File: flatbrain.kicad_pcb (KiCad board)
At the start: 2 copper layers, 272.2 x 143 mm, 108 parts, among them J1 OLED, SW1 SW_Push, SW41 Rotary_Encoder_Switch, SW42 Rotary_Encoder_Switch, U1 Elite-C

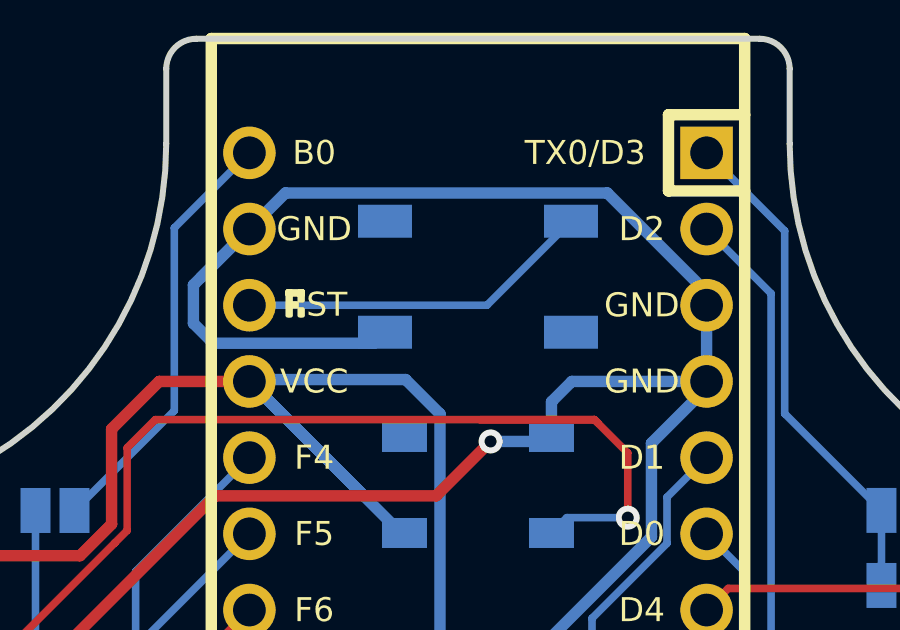
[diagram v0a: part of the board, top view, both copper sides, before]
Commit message: Remove gerber file
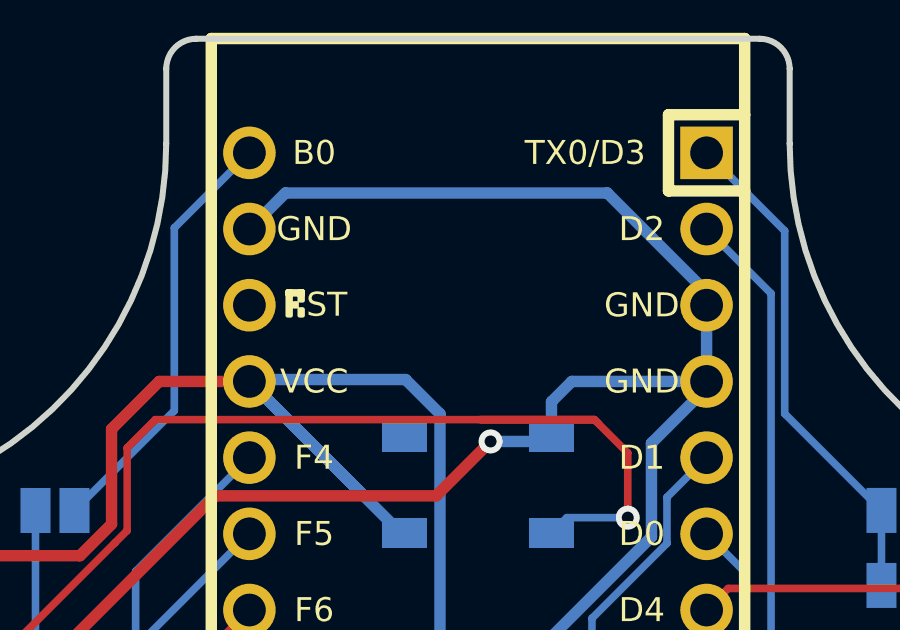
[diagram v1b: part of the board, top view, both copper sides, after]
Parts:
- removed SW1: SW_Push, random-keyboard-parts:SKQG-1155865
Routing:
- net GND: track 835.1 -> 821.6 mm
- net RST: track 11.9 -> 0.00 mm

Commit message: Update the outline with the new design
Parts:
- moved D46 17.2 mm to (221.4, 96.0)
- moved D40 17.2 mm to (120.0, 137.6)
- moved D37 16.7 mm to (74.4, 96.0)
- moved D35 13.1 mm to (247.3, 69.6), turned to 208 degrees
- moved D36 11.3 mm to (264.1, 60.7), turned to 208 degrees
- moved D25 11.2 mm to (31.7, 60.7), turned to 332 degrees
- moved LED7 7.64 mm to (32.1, 75.9)
- moved LED3 7.17 mm to (263.7, 75.9)
- moved LED6 3.94 mm to (85.2, 108.3)
- moved LED4 3.72 mm to (210.6, 108.3)
- moved LED5 1.92 mm to (147.9, 141.9)
- moved D3 0.95 mm to (92.7, 40.4)
- moved MX39 0.95 mm to (112.9, 127.6)
- moved J1 0.95 mm to (151.7, 53.1)
- moved D5 0.95 mm to (126.1, 58.7)
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- renumbered JP1 to Elite-c, JP2 to Elite-c, JP3 to Pro-micro
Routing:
- net GND: track 821.6 -> 799.8 mm
- net ROW3: track 299.4 -> 317.9 mm
- net Net-(D36-Pad2): track 11.3 -> 3.44 mm
- net VCC: track 701.1 -> 693.7 mm
- net Net-(LED2-Pad2): track 65.9 -> 59.2 mm
- net Net-(LED5-Pad2): track 90.7 -> 85.2 mm
- net Net-(D46-Pad2): track 11.3 -> 6.20 mm
- net Net-(D37-Pad2): track 6.20 -> 11.3 mm
- net Net-(D40-Pad2): track 6.20 -> 11.3 mm
- net COL0: track 147.7 -> 143.6 mm
- net Net-(LED8-Pad2): track 60.7 -> 56.9 mm
- net ROW2: track 371.5 -> 375.2 mm
- net Net-(D25-Pad2): track 7.25 -> 3.97 mm
- net Net-(D35-Pad2): track 6.20 -> 3.44 mm
- net COL3: track 149.5 -> 152.0 mm
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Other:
- board size 272.2 x 143 mm -> 268.7 x 141.1 mm

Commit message: Add choc support
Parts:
- MX1, MX10, MX11, MX12, MX13, MX14, MX15, MX16, MX17, MX18, MX19, MX2, MX20, MX21, MX22, MX23, MX24, MX25, MX26, MX27, MX28, MX29, MX3, MX30, MX31, MX32, MX33, MX34, MX35, MX36, MX37, MX38, MX39, MX4, MX40, MX43, MX44, MX45, MX46, MX5, MX6, MX7, MX8, MX9: footprint parts:mx_1u -> parts:mxchoc_1u
- SW41, SW42: footprint parts:rotary_x_mx -> parts:rotary_x_mxchoc
- moved MX22 3.61 mm to (219.0, 56.9)
- moved LED3 3.61 mm to (263.4, 79.5)
- moved MX13 3.61 mm to (34.7, 53.8)
- moved D10 3.61 mm to (217.3, 36.2)
- moved MX37 3.61 mm to (81.4, 103.4)
- moved D29 3.61 mm to (107.9, 96.0)
- moved D44 3.61 mm to (187.5, 124.6)
- moved D6 3.61 mm to (141.5, 73.4)
- moved D28 3.61 mm to (94.1, 81.3)
- moved MX27 3.61 mm to (67.2, 73.8)
- moved MX33 3.61 mm to (208.3, 77.4)
- moved D26 3.61 mm to (49.9, 83.4)
- moved D5 3.61 mm to (125.8, 62.3)
- moved D8 3.61 mm to (183.9, 54.6)
- moved MX20 3.61 mm to (185.6, 75.3)
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- renumbered Elite-c to elite-c, Pro-micro to pro-micro
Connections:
- net RST renamed Net-(U1-Pad22)
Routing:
- net COL4: track 132.3 -> 162.5 mm
- net Net-(LED8-Pad2): track 56.9 -> 83.3 mm
- net COL1: track 174.9 -> 198.2 mm
- net COL8: track 144.8 -> 165.9 mm
- net COL5: track 87.1 -> 105.6 mm
- net COL6: track 86.9 -> 105.2 mm
- net COL7: track 127.1 -> 145.1 mm
- net COL9: track 151.9 -> 169.2 mm
- net COL10: track 174.9 -> 191.2 mm
- net COL11: track 138.7 -> 154.9 mm
- net COL2: track 159.9 -> 175.4 mm
- net COL3: track 152.0 -> 166.7 mm
- net COL0: track 143.6 -> 154.7 mm
- net ROW1: track 331.4 -> 341.8 mm
- net Net-(LED2-Pad2): track 59.2 -> 67.1 mm
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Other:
- outline, holes or cut-outs redrawn

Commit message: wip: switches placed, matrix change
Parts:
- removed D31, D40, D41, D42, D43, D44, D45, D46: D_Small, Keebio-Parts:Diode-Hybrid-Back
- removed the D38 at (104.8, 121.5)
- removed MX31, MX35, MX36, MX40, MX43, MX44, MX45, MX46: MX-NoLED, parts:mxchoc_1u
- removed SW41, SW42: Rotary_Encoder_Switch, parts:rotary_x_mxchoc
- removed elite-c (x2), pro-micro: Jumper_NO_Small, Jumper:SolderJumper-2_P1.3mm_Open_Pad1.0x1.5mm
- added D38: D_Small, Keebio-Parts:Diode-dual, F.Cu at (315.5, 104.4)
- added D38: D_Small, Keebio-Parts:Diode-dual, F.Cu at (294.7, 99.1)
- D1, D10, D11, D12, D13, D14, D15, D16, D17, D18, D19, D2, D20, D21, D22, D23, D24, D25, D26, D27, D28, D29, D3, D30, D32, D33, D34, D35, D36, D37, D39, D4, D5, D6, D7, D8, D9: footprint Keebio-Parts:Diode-Hybrid-Back -> Keebio-Parts:Diode-dual
- MX1, MX10, MX11, MX12, MX13, MX14, MX15, MX16, MX17, MX18, MX19, MX2, MX20, MX21, MX22, MX23, MX24, MX25, MX26, MX27, MX28, MX29, MX3, MX30, MX32, MX33, MX34, MX37, MX38, MX39, MX4, MX5, MX6, MX7, MX8, MX9: footprint parts:mxchoc_1u -> parts:mix_1u
- U1: moved to F.Cu
- moved D13 328.8 mm to (367.5, 104.4), turned to 0 degrees
- moved D14 321.0 mm to (377.9, 101.7), turned to 0 degrees
- moved D26 307.6 mm to (357.1, 99.1), turned to 0 degrees
- moved D25 307.5 mm to (336.3, 104.4), turned to 0 degrees
- moved D15 296.9 mm to (377.9, 99.1), turned to 0 degrees
- moved LED8 281.3 mm to (329.4, 77.0), turned to 0 degrees
- moved D1 279.8 mm to (325.9, 99.1), turned to 0 degrees
- moved D27 273.2 mm to (346.7, 101.7), turned to 0 degrees
- moved LED7 270.6 mm to (302.4, 82.5), turned to 0 degrees
- moved D28 263.7 mm to (357.1, 101.7), turned to 0 degrees
- moved D2 241.1 mm to (305.1, 99.1), turned to 0 degrees
- moved LED9 234.0 mm to (330.2, 65.1), turned to 0 degrees
- moved D3 229.8 mm to (315.5, 99.1), turned to 0 degrees
- moved D16 223.3 mm to (321.8, 19.3), turned to 0 degrees
- moved D30 223.2 mm to (346.7, 99.1), turned to 0 degrees
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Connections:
- D11 pad 1: ROW0 -> ROW1
- D12 pad 1: ROW0 -> ROW1
- D21 pad 1: ROW1 -> ROW2
- D22 pad 1: ROW1 -> ROW2
- D23 pad 1: ROW1 -> ROW2
- D24 pad 1: ROW1 -> ROW2
- D32 pad 1: ROW2 -> ROW3
- D33 pad 1: ROW2 -> ROW3
- D34 pad 1: ROW2 -> ROW3
- D35 pad 1: ROW2 -> ROW3
- D36 pad 1: ROW2 -> ROW3
- MX11 pad 1: COL10 -> COL0
- MX12 pad 1: COL11 -> COL1
- MX13 pad 1: COL0 -> COL2
- MX14 pad 1: COL1 -> COL3
- MX15 pad 1: COL2 -> COL4
- MX16 pad 1: COL3 -> COL5
- MX17 pad 1: COL4 -> COL6
- MX18 pad 1: COL5 -> COL7
- MX19 pad 1: COL6 -> COL8
- MX20 pad 1: COL7 -> COL9
- MX21 pad 1: COL8 -> COL0
- MX22 pad 1: COL9 -> COL1
- MX23 pad 1: COL10 -> COL2
- MX24 pad 1: COL11 -> COL3
- MX25 pad 1: COL0 -> COL4
- MX26 pad 1: COL1 -> COL5
- MX27 pad 1: COL2 -> COL6
- MX28 pad 1: COL3 -> COL7
- MX29 pad 1: COL4 -> COL8
- MX30 pad 1: COL5 -> COL9
- MX32 pad 1: COL7 -> COL1
- MX33 pad 1: COL8 -> COL2
- MX34 pad 1: COL9 -> COL3
- MX37 pad 1: COL1 -> COL6
- MX38 pad 1: COL2 -> COL7
- MX39 pad 1: COL3 -> COL8
- U1 pad 1: Net-(JP2-Pad2) -> LED
- U1 pad 7: COL11 -> ROW0
- U1 pad 8: COL10 -> Net-(U1-Pad8)
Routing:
- net GND: track 797.5 -> 0.00 mm, vias 2 -> 0
- net VCC: track 693.6 -> 0.00 mm, vias 1 -> 0
- net ROW2: track 378.1 -> 0.00 mm, vias 1 -> 0
- net ROW1: track 341.8 -> 0.00 mm, vias 1 -> 0
- net ROW3: track 320.2 -> 0.00 mm, vias 1 -> 0
- net ROW0: track 303.9 -> 0.00 mm
- net COL1: track 198.2 -> 0.00 mm
- net COL10: track 191.2 -> 0.00 mm
- net COL2: track 175.4 -> 0.00 mm
- net COL9: track 169.2 -> 0.00 mm
- net COL3: track 166.7 -> 0.00 mm
- net COL8: track 165.9 -> 0.00 mm
- net COL4: track 162.5 -> 0.00 mm
- net COL11: track 154.9 -> 0.00 mm
- net COL0: track 154.7 -> 0.00 mm
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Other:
- board size 268.7 x 141.1 mm -> 239 x 128.4 mm
- board text removed: "Designed by louckousse"
- board text removed: "JLCJLCJLCJLC"

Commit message: everything is placed
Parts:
- removed D36: D_Small, Keebio-Parts:Diode-dual
- removed the D38 at (315.5, 104.4)
- removed the D38 at (294.7, 99.1)
- added D38: D_Small, Keebio-Parts:Diode-dual, F.Cu at (229.4, 114.2)
- added J2: Conn_01x05, Kicad-Footprints:pimoroni_trackball, F.Cu at (161.8, 114.7)
- added SW1: Rotary_Encoder_Switch, parts:rotary_x_mx, F.Cu at (134.6, 124.6)
- U1: moved to B.Cu
- moved D24 316.4 mm to (61.5, 108.5), turned to 242 degrees
- moved D22 311.3 mm to (56.2, 105.7), turned to 242 degrees
- moved D23 308.7 mm to (58.9, 107.1), turned to 242 degrees
- moved D14 298.0 mm to (79.9, 105.9), turned to 242 degrees
- moved D15 295.4 mm to (82.6, 107.3), turned to 242 degrees
- moved D21 290.6 mm to (53.6, 104.3), turned to 242 degrees
- moved D13 290.2 mm to (77.3, 104.4), turned to 242 degrees
- moved LED8 283.5 mm to (48.8, 117.1), turned to 332 degrees
- moved D12 282.4 mm to (74.6, 103.0), turned to 242 degrees
- moved LED9 282.1 mm to (48.8, 46.0), turned to 62 degrees
- moved D25 272.2 mm to (64.2, 109.9), turned to 242 degrees
- moved D32 269.6 mm to (66.8, 111.3), turned to 242 degrees
- moved D1 267.2 mm to (58.8, 94.6), turned to 242 degrees
- moved D34 264.6 mm to (72.1, 114.2), turned to 242 degrees
- moved D33 256.6 mm to (69.5, 112.7), turned to 242 degrees
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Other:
- board size 239 x 128.4 mm -> 249.8 x 129.3 mm

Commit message: first half done
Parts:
- D1, D11, D12, D13, D14, D15, D2, D21, D22, D23, D24, D25, D3, D32, D33, D34, D35, D4, D5: footprint Keebio-Parts:Diode-dual -> Keebio-Parts:Diode-Hybrid-Back; moved to B.Cu
- D10, D16, D17, D18, D19, D20, D26, D27, D28, D29, D30, D37, D38, D39, D6, D7, D8, D9: footprint Keebio-Parts:Diode-dual -> Keebio-Parts:Diode-Hybrid-Back
- moved LED5 54.7 mm to (205.4, 153.1)
- moved LED6 45.9 mm to (155.4, 158.1)
- moved D5 19.8 mm to (86.5, 110.2)
- moved D4 16.8 mm to (81.2, 107.4)
- moved D3 13.8 mm to (75.9, 104.6)
- moved D25 13.8 mm to (76.0, 117.1)
- moved D24 10.8 mm to (70.7, 114.3)
- moved D2 10.8 mm to (70.6, 101.8)
- moved D11 10.2 mm to (63.3, 96.2)
- moved D34 10.2 mm to (63.5, 108.8)
- moved D1 7.86 mm to (65.3, 99.0)
- moved D23 7.86 mm to (65.4, 111.5)
- moved D32 7.85 mm to (74.1, 114.4)
- moved D12 7.21 mm to (68.6, 99.1)
- moved D22 4.89 mm to (60.1, 108.7)
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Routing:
- net GND: track 0.00 -> 461.5 mm
- net VCC: track 0.00 -> 444.3 mm
- net COL2: track 0.00 -> 165.7 mm
- net COL3: track 0.00 -> 161.8 mm
- net COL1: track 0.00 -> 159.9 mm
- net COL4: track 0.00 -> 115.9 mm
- net Net-(D34-Pad2): track 0.00 -> 110.3 mm
- net COL0: track 0.00 -> 88.9 mm
- net Net-(D5-Pad2): track 0.00 -> 86.8 mm
- net Net-(D33-Pad2): track 0.00 -> 84.4 mm
- net Net-(LED8-Pad2): track 0.00 -> 80.0 mm
- net Net-(D4-Pad2): track 0.00 -> 77.9 mm
- net Net-(D3-Pad2): track 0.00 -> 77.0 mm
- net Net-(D35-Pad2): track 0.00 -> 71.2 mm
- net Net-(D25-Pad2): track 0.00 -> 70.2 mm
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
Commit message: all route done
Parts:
- D10, D16, D17, D18, D19, D20, D26, D27, D28, D29, D30, D37, D38, D39, D6, D7, D8, D9: moved to B.Cu
- moved D16 22.4 mm to (215.6, 109.2)
- moved D17 19.4 mm to (220.9, 106.4)
- moved D18 16.5 mm to (226.2, 103.6)
- moved D39 14.0 mm to (222.7, 116.2)
- moved D19 13.6 mm to (231.5, 100.8)
- moved D26 13.6 mm to (226.1, 116.1)
- moved D27 10.7 mm to (231.4, 113.3)
- moved D20 10.7 mm to (236.8, 98.0)
- moved D10 9.28 mm to (238.8, 95.2)
- moved MX19 8.68 mm to (221.7, 66.3)
- moved D35 8.68 mm to (70.7, 116.2)
- moved MX37 8.68 mm to (169.0, 148.5)
- moved MX6 8.68 mm to (163.7, 78.9)
- moved D21 8.68 mm to (49.5, 105.0)
- moved D4 8.68 mm to (72.5, 106.4)
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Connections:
- net ENC1A renamed ENCA
- net ENC1B renamed ENCB
- net ENC2A renamed Net-(U1-Pad25)
- net ENC2B renamed Net-(U1-Pad26)
- U1 pad 10: COL8 -> COL5
- U1 pad 11: COL7 -> ROW2
- U1 pad 12: COL6 -> ROW3
- U1 pad 13: COL5 -> Net-(U1-Pad13)
- U1 pad 14: COL4 -> ROW1
- U1 pad 15: COL3 -> ROW0
- U1 pad 16: COL2 -> COL4
- U1 pad 17: COL1 -> COL3
- U1 pad 18: COL0 -> COL2
- U1 pad 19: ROW3 -> COL1
- U1 pad 2: ROW1 -> COL9
- U1 pad 20: ROW2 -> COL0
- U1 pad 7: ROW0 -> COL8
- U1 pad 8: Net-(U1-Pad8) -> COL7
- U1 pad 9: COL9 -> COL6
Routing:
- net ROW1: track 24.0 -> 396.2 mm, vias 0 -> 1
- net ROW0: track 24.0 -> 388.0 mm, vias 0 -> 1
- net ROW2: track 21.6 -> 329.5 mm, vias 0 -> 1
- net ROW3: track 18.0 -> 309.7 mm, vias 0 -> 1
- net GND: track 461.5 -> 703.8 mm
- net VCC: track 444.3 -> 679.5 mm
- net COL8: track 0.00 -> 210.5 mm
- net COL7: track 0.00 -> 197.6 mm
- net COL6: track 0.00 -> 179.1 mm
- net COL9: track 0.00 -> 176.1 mm
- net COL5: track 0.00 -> 106.5 mm
- net COL0: track 88.9 -> 180.6 mm
- net Net-(D8-Pad2): track 0.00 -> 90.5 mm
- net ENCA: track 0.00 -> 89.9 mm
- net Net-(D6-Pad2): track 0.00 -> 85.6 mm
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
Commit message: rev3 is done
add a rotary
add silk
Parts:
- added D30: D_Small, Keebio-Parts:Diode-Hybrid-Back, B.Cu at (243.7, 104.6)
- added G***: LOGO, cc:cc, F.Cu at (146.5, 49.9)
- added SW2: Rotary_Encoder_Switch, parts:rotary_full, F.Cu at (162.7, 124.8)
- SW1: footprint parts:rotary_x_mx -> parts:rotary_full
- moved D24 0.45 mm to (61.9, 112.9)
- moved MX37 0.45 mm to (168.8, 148.1)
- moved D34 0.45 mm to (54.6, 107.4)
- moved LED5 0.45 mm to (196.5, 151.7)
- moved D20 0.45 mm to (236.6, 97.6)
- moved D4 0.45 mm to (72.3, 106.0)
- moved D14 0.45 mm to (70.4, 103.3)
- moved D19 0.45 mm to (231.3, 100.4)
- moved D39 0.45 mm to (225.9, 115.7)
- moved D9 0.45 mm to (233.2, 97.7)
- moved MX27 0.45 mm to (197.0, 101.1)
- moved D11 0.45 mm to (54.5, 94.9)
- moved D12 0.45 mm to (59.8, 97.7)
- moved MX9 0.45 mm to (212.6, 49.1)
- moved MX12 0.45 mm to (71.5, 65.9)
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- renumbered D38 to D26, D37 to D27, D29 to D28, D30 to D29, D39 to D36, D28 to D37, D27 to D38, D26 to D39
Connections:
- D26 pad 1: ROW3 -> ROW2
- D26 pad 2: Net-(D38-Pad2) -> Net-(D26-Pad2)
- D27 pad 1: ROW3 -> ROW2
- D27 pad 2: Net-(D37-Pad2) -> Net-(D27-Pad2)
- D28 pad 2: Net-(D29-Pad2) -> Net-(D28-Pad2)
- D29 pad 2: Net-(D30-Pad2) -> Net-(D29-Pad2)
- D36 pad 2: Net-(D39-Pad2) -> Net-(D36-Pad2)
- D37 pad 1: ROW2 -> ROW3
- D37 pad 2: Net-(D28-Pad2) -> Net-(D37-Pad2)
- D38 pad 1: ROW2 -> ROW3
- D38 pad 2: Net-(D27-Pad2) -> Net-(D38-Pad2)
- D39 pad 1: ROW2 -> ROW3
- D39 pad 2: Net-(D26-Pad2) -> Net-(D39-Pad2)
- SW1 pad A: ENCA -> ENC1A
- SW1 pad B: ENCB -> ENC1B
- U1 pad 25: Net-(U1-Pad25) -> ENC2A
- U1 pad 26: Net-(U1-Pad26) -> ENC2B
- U1 pad 28: ENCA -> ENC1B
- U1 pad 29: ENCB -> ENC1A
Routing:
- net ENCA: track 89.9 -> 0.00 mm
- net ENC1A: track 0.00 -> 84.6 mm
- net ENC1B: track 0.00 -> 81.7 mm
- net ENC2A: track 0.00 -> 80.9 mm
- net ENCB: track 79.6 -> 0.00 mm
- net ENC2B: track 0.00 -> 74.6 mm
- net Net-(D36-Pad2): track 0.00 -> 67.2 mm
- net GND: track 703.8 -> 736.3 mm
- net COL5: track 106.5 -> 138.3 mm
- net ROW2: track 329.5 -> 342.8 mm
- net ROW3: track 309.7 -> 321.7 mm
- net Net-(D29-Pad2): track 43.4 -> 35.4 mm
- net SCL: track 76.6 -> 83.1 mm
- net Net-(D30-Pad2): track 50.2 -> 43.9 mm
- net SDA: track 84.3 -> 80.5 mm
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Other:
- board text added: "BISOUS"
